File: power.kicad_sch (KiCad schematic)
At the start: 40 parts, among them J11 Conn_01x02_Pin, J2 Conn_01x02_Pin, Q1 PMOS, Q2 PMOS, Q3 NMOS, U1 LFE5U-12F-6BG256C, U3 AMS1117-3.3, U4 TPS74611PQWDRBRQ1, U5 XC6206P252MR

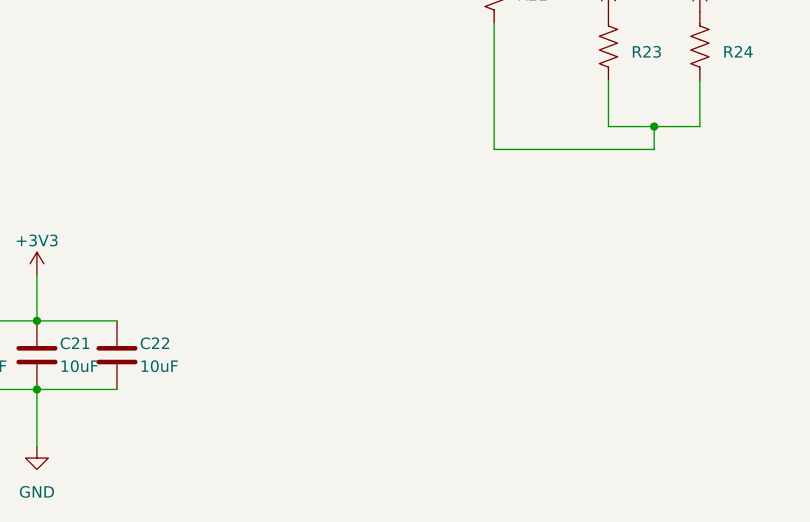
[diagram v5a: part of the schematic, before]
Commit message: Silkscreen, more power
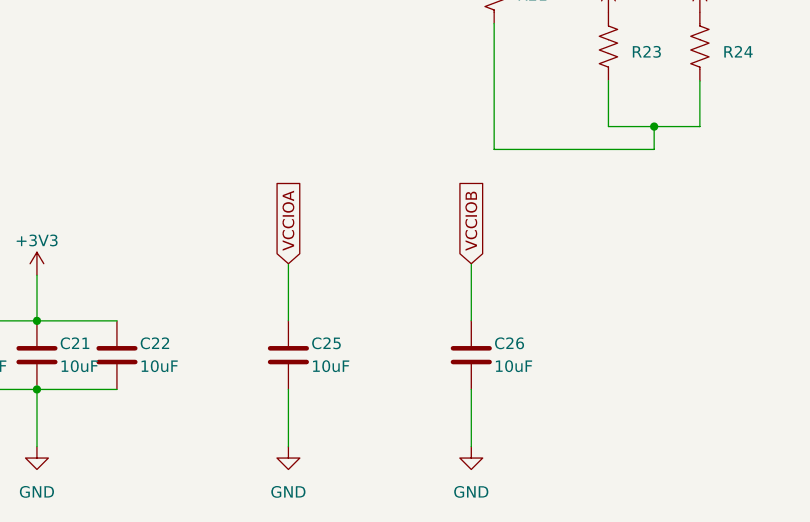
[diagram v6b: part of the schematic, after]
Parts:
- added C25, C26: 10uF, Capacitor_SMD:C_0805_2012Metric, symbol Device:C
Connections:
- net GND: now also C25.2, C26.2
- net VCCIOA: now also C25.1
- net VCCIOB: now also C26.1
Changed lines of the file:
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@@
+    (stroke (width 0) (type default))
+  )
+  (wire (pts (xy 195.58 135.89) (xy 195.58 142.24))
+    (stroke (width 0) (type default))
+  )
+  (wire (pts (xy 215.9 135.89) (xy 215.9 142.24))
+    (stroke (width 0) (type default))
+  )
+  (wire (pts (xy 215.9 121.92) (xy 215.9 128.27))
     (stroke (width 0) (type default))
   )
@@
   )
   (wire (pts (xy 194.31 69.85) (xy 196.85 69.85))
+    (stroke (width 0) (type default))
+  )
+  (wire (pts (xy 195.58 121.92) (xy 195.58 128.27))
     (stroke (width 0) (type default))
   )
@@
     )
   )
+  (global_label "VCCIOA" (shape input) (at 195.58 121.92 90) (fields_autoplaced)
+    (effects (font (size 1.27 1.27)) (justify left))
+    (property "Intersheetrefs" "${INTERSHEET_REFS}" (at 195.58 112.3617 90)
+      (effects (font (size 1.27 1.27)) (justify left) hide)
+    )
+  )
   (global_label "5VREGIN" (shape input) (at 90.17 125.73 0) (fields_autoplaced)
     (effects (font (size 1.27 1.27)) (justify left))
@@
     )
   )
+  (global_label "VCCIOB" (shape input) (at 215.9 121.92 90) (fields_autoplaced)
+    (effects (font (size 1.27 1.27)) (justify left))
+    (property "Intersheetrefs" "${INTERSHEET_REFS}" (at 215.9 112.1803 90)
+      (effects (font (size 1.27 1.27)) (justify left) hide)
+    )
+  )
   (global_label "2V5REGOUT" (shape input) (at 146.05 69.85 90) (fields_autoplaced)
     (effects (font (size 1.27 1.27)) (justify left))
@@
     )
   )
+  (symbol (lib_id "power:GND") (at 195.58 142.24 0) (unit 1)
+    (in_bom yes) (on_board yes) (dnp no) (fields_autoplaced)
+    (property "Reference" "#PWR015" (at 195.58 148.59 0)
+      (effects (font (size 1.27 1.27)) hide)
+    )
+    (property "Value" "GND" (at 195.58 147.32 0)
+      (effects (font (size 1.27 1.27)))
+    )
+    (property "Footprint" "" (at 195.58 142.24 0)
+      (effects (font (size 1.27 1.27)) hide)
+    )
+    (property "Datasheet" "" (at 195.58 142.24 0)
+      (effects (font (size 1.27 1.27)) hide)
+    )
+    (pin "1")
+    (instances
+      (project "daughterboard"
+        (path "/dce8b7ce-114c-4680-a1bd-14f36a94838a/233da297-15ca-4163-a51b-09f27dce3135"
+          (reference "#PWR015") (unit 1)
+        )
+      )
+    )
+  )
   (symbol (lib_id "Device:C") (at 162.56 38.1 0) (unit 1)
     (in_bom yes) (on_board yes) (dnp no) (fields_autoplaced)
@@
         (path "/dce8b7ce-114c-4680-a1bd-14f36a94838a/233da297-15ca-4163-a51b-09f27dce3135"
           (reference "C2") (unit 1)
+        )
+      )
+    )
+  )
+  (symbol (lib_id "Device:C") (at 195.58 132.08 0) (unit 1)
+    (in_bom yes) (on_board yes) (dnp no)
+    (property "Reference" "C25" (at 198.12 130.81 0)
+      (effects (font (size 1.27 1.27)) (justify left))
+    )
+    (property "Value" "10uF" (at 198.12 133.35 0)
+      (effects (font (size 1.27 1.27)) (justify left))
+    )
+    (property "Footprint" "Capacitor_SMD:C_0805_2012Metric" (at 196.5452 135.89 0)
+      (effects (font (size 1.27 1.27)) hide)
+    )
+    (property "Datasheet" "~" (at 195.58 132.08 0)
+      (effects (font (size 1.27 1.27)) hide)
+    )
+    (pin "1")
+    (pin "2")
+    (instances
+      (project "daughterboard"
+        (path "/dce8b7ce-114c-4680-a1bd-14f36a94838a/233da297-15ca-4163-a51b-09f27dce3135"
+          (reference "C25") (unit 1)
+        )
+        (path "/dce8b7ce-114c-4680-a1bd-14f36a94838a/60bc7ad5-be18-49b3-905c-1be058d9dfc0"
+          (reference "C9") (unit 1)
         )
       )
@@
         )
       )
+    )
+  )
+  (symbol (lib_id "power:GND") (at 215.9 142.24 0) (unit 1)
+    (in_bom yes) (on_board yes) (dnp no) (fields_autoplaced)
+    (property "Reference" "#PWR027" (at 215.9 148.59 0)
+      (effects (font (size 1.27 1.27)) hide)
+    )
+    (property "Value" "GND" (at 215.9 147.32 0)
+      (effects (font (size 1.27 1.27)))
+    )
+    (property "Footprint" "" (at 215.9 142.24 0)
+      (effects (font (size 1.27 1.27)) hide)
+    )
+    (property "Datasheet" "" (at 215.9 142.24 0)
+      (effects (font (size 1.27 1.27)) hide)
+    )
+    (pin "1")
+    (instances
+      (project "daughterboard"
+        (path "/dce8b7ce-114c-4680-a1bd-14f36a94838a/233da297-15ca-4163-a51b-09f27dce3135"
+          (reference "#PWR027") (unit 1)
+        )
+      )
+    )
+  )
+  (symbol (lib_id "Device:C") (at 215.9 132.08 0) (unit 1)
+    (in_bom yes) (on_board yes) (dnp no)
+    (property "Reference" "C26" (at 218.44 130.81 0)
+      (effects (font (size 1.27 1.27)) (justify left))
+    )
+    (property "Value" "10uF" (at 218.44 133.35 0)
+      (effects (font (size 1.27 1.27)) (justify left))
+    )
+    (property "Footprint" "Capacitor_SMD:C_0805_2012Metric" (at 216.8652 135.89 0)
+      (effects (font (size 1.27 1.27)) hide)
+    )
+    (property "Datasheet" "~" (at 215.9 132.08 0)
+      (effects (font (size 1.27 1.27)) hide)
+    )
+    (pin "1")
+    (pin "2")
+    (instances
+      (project "daughterboard"
+        (path "/dce8b7ce-114c-4680-a1bd-14f36a94838a/233da297-15ca-4163-a51b-09f27dce3135"
+          (reference "C26") (unit 1)
+        )
+        (path "/dce8b7ce-114c-4680-a1bd-14f36a94838a/60bc7ad5-be18-49b3-905c-1be058d9dfc0"
+          (reference "C9") (unit 1)
+        )
+      )

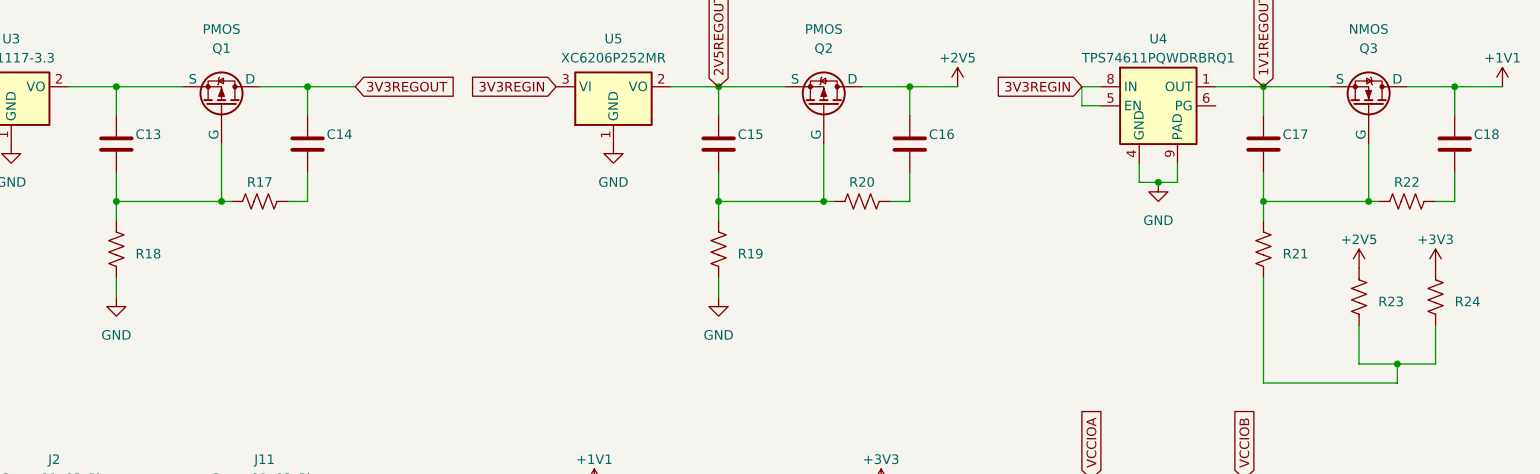
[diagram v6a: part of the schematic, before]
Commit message: Values for slow start circuitry
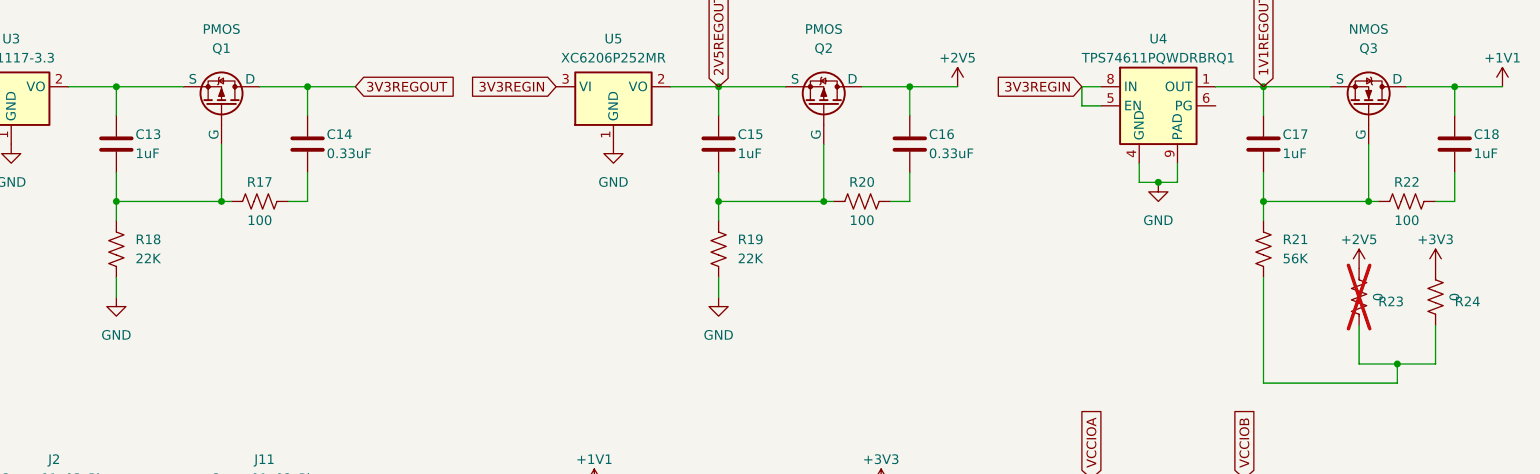
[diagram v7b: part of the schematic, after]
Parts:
- C13, C15, C17, C18: value ~ -> 1uF
- C14, C16: value ~ -> 0.33uF
- R17, R20, R22: value ~ -> 100
- R18, R19: value ~ -> 22K
- R21: value ~ -> 56K
- R23: value ~ -> 0; now not fitted
- R24: value ~ -> 0
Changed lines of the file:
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@@
   )
   (symbol (lib_id "Device:R_US") (at 231.14 97.79 180) (unit 1)
-    (in_bom yes) (on_board yes) (dnp no) (fields_autoplaced)
+    (in_bom yes) (on_board yes) (dnp yes) (fields_autoplaced)
     (property "Reference" "R23" (at 233.68 98.425 0)
       (effects (font (size 1.27 1.27)) (justify right))
     )
-    (property "Value" "~" (at 233.68 97.79 90)
+    (property "Value" "0" (at 233.68 97.79 90)
       (effects (font (size 1.27 1.27)))
     )
@@
       (effects (font (size 1.27 1.27)) (justify left))
     )
-    (property "Value" "~" (at 93.98 78.74 0)
+    (property "Value" "0.33uF" (at 93.98 78.74 0)
       (effects (font (size 1.27 1.27)) (justify left))
     )
@@
       (effects (font (size 1.27 1.27)) (justify right))
     )
-    (property "Value" "~" (at 243.84 97.79 90)
+    (property "Value" "0" (at 243.84 97.79 90)
       (effects (font (size 1.27 1.27)))
     )
@@
   )
   (symbol (lib_id "Device:R_US") (at 85.09 85.09 270) (unit 1)
-    (in_bom yes) (on_board yes) (dnp no) (fields_autoplaced)
+    (in_bom yes) (on_board yes) (dnp no)
     (property "Reference" "R17" (at 85.09 82.55 90)
       (effects (font (size 1.27 1.27)))
     )
-    (property "Value" "~" (at 85.09 82.55 90)
+    (property "Value" "100" (at 85.09 87.63 90)
       (effects (font (size 1.27 1.27)))
     )
@@
       (effects (font (size 1.27 1.27)) (justify left))
     )
-    (property "Value" "~" (at 246.38 78.74 0)
+    (property "Value" "1uF" (at 246.38 78.74 0)
       (effects (font (size 1.27 1.27)) (justify left))
     )
@@
   )
   (symbol (lib_id "Device:R_US") (at 237.49 85.09 270) (unit 1)
-    (in_bom yes) (on_board yes) (dnp no) (fields_autoplaced)
+    (in_bom yes) (on_board yes) (dnp no)
     (property "Reference" "R22" (at 237.49 82.55 90)
       (effects (font (size 1.27 1.27)))
     )
-    (property "Value" "~" (at 237.49 82.55 90)
+    (property "Value" "100" (at 237.49 87.63 90)
       (effects (font (size 1.27 1.27)))
     )
@@
   )
   (symbol (lib_id "Device:R_US") (at 146.05 91.44 180) (unit 1)
-    (in_bom yes) (on_board yes) (dnp no) (fields_autoplaced)
-    (property "Reference" "R19" (at 148.59 92.075 0)
+    (in_bom yes) (on_board yes) (dnp no)
+    (property "Reference" "R19" (at 148.59 90.17 0)
       (effects (font (size 1.27 1.27)) (justify right))
     )
-    (property "Value" "~" (at 148.59 93.345 0)
+    (property "Value" "22K" (at 148.59 92.71 0)
       (effects (font (size 1.27 1.27)) (justify right))
     )
@@
       (effects (font (size 1.27 1.27)) (justify left))
     )
-    (property "Value" "~" (at 68.58 78.74 0)
+    (property "Value" "1uF" (at 68.58 78.74 0)
       (effects (font (size 1.27 1.27)) (justify left))
     )
@@
   )
   (symbol (lib_id "Device:R_US") (at 165.1 85.09 270) (unit 1)
-    (in_bom yes) (on_board yes) (dnp no) (fields_autoplaced)
+    (in_bom yes) (on_board yes) (dnp no)
     (property "Reference" "R20" (at 165.1 82.55 90)
       (effects (font (size 1.27 1.27)))
     )
-    (property "Value" "~" (at 165.1 82.55 90)
+    (property "Value" "100" (at 165.1 87.63 90)
       (effects (font (size 1.27 1.27)))
     )
@@
   )
   (symbol (lib_id "Device:R_US") (at 218.44 91.44 180) (unit 1)
-    (in_bom yes) (on_board yes) (dnp no) (fields_autoplaced)
-    (property "Reference" "R21" (at 220.98 92.075 0)
+    (in_bom yes) (on_board yes) (dnp no)
+    (property "Reference" "R21" (at 220.98 90.17 0)
       (effects (font (size 1.27 1.27)) (justify right))
     )
-    (property "Value" "~" (at 220.98 93.345 0)
+    (property "Value" "56K" (at 220.98 92.71 0)
       (effects (font (size 1.27 1.27)) (justify right))
     )
@@
       (effects (font (size 1.27 1.27)) (justify left))
     )
-    (property "Value" "~" (at 173.99 78.74 0)
+    (property "Value" "0.33uF" (at 173.99 78.74 0)
       (effects (font (size 1.27 1.27)) (justify left))
     )
@@
       (effects (font (size 1.27 1.27)) (justify left))
     )
-    (property "Value" "~" (at 148.59 78.74 0)
+    (property "Value" "1uF" (at 148.59 78.74 0)
       (effects (font (size 1.27 1.27)) (justify left))
     )
@@
   )
   (symbol (lib_id "Device:R_US") (at 66.04 91.44 180) (unit 1)
-    (in_bom yes) (on_board yes) (dnp no) (fields_autoplaced)
-    (property "Reference" "R18" (at 68.58 92.075 0)
+    (in_bom yes) (on_board yes) (dnp no)
+    (property "Reference" "R18" (at 68.58 90.17 0)
       (effects (font (size 1.27 1.27)) (justify right))
     )
-    (property "Value" "~" (at 68.58 93.345 0)
+    (property "Value" "22K" (at 68.58 92.71 0)
       (effects (font (size 1.27 1.27)) (justify right))
     )
@@
       (effects (font (size 1.27 1.27)) (justify left))
     )
-    (property "Value" "~" (at 220.98 78.74 0)
-      (effects (font (size 1.27 1.27)) (justify left))
-    )
+    (property "Value" "1uF" (at 220.98 78.74 0)
+      (effects (font (size 1.27 1.27)) (justify left))
+    )
